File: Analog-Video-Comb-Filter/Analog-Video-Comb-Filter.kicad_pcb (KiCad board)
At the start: 2 copper layers, 51.5 x 104.1 mm, 97 parts, among them J1 12VDC(+), J2 SVHS, J3 CVBS, Q1 BC548, Q10 BC548, Q2 BC548, Q3 BC558, Q4 BC558, Q5 BC548, Q6 BC548, Q7 BC548, Q8 BC558, Q9 BC548, U1 L7805, U2 SAA4961, U3 MC44144, U4 74HC04, U5 LM1881, Y1 See table

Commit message: Replaced RCA connector footprint, added gerber files, fixed README
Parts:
- added J4: CV-IN, Custom_Footprints:Keystone_973, F.Cu at (124.2, 90.2)
- J3: value CVBS -> CV-OUT; footprint Custom_Footprints:RCA_Dual_Switch -> Custom_Footprints:Keystone_973
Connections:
- J3 pad 1: /CVBS-IN -> /CVBS-OUT
- J3 pad 3: /CVBS-OUT -> unconnected-(J3-Sw-Pad3)
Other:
- board text removed: "IN"

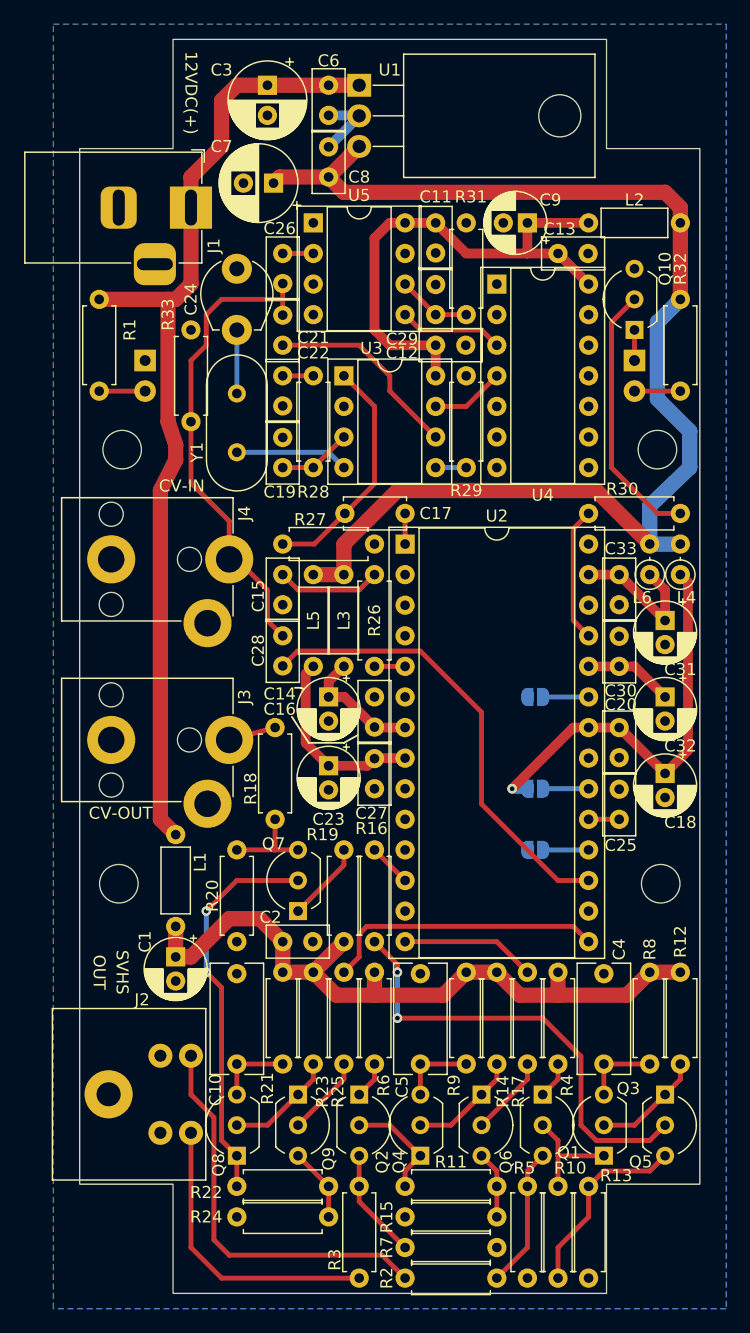
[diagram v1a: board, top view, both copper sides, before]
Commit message: Added alternative footprint for SAA4963
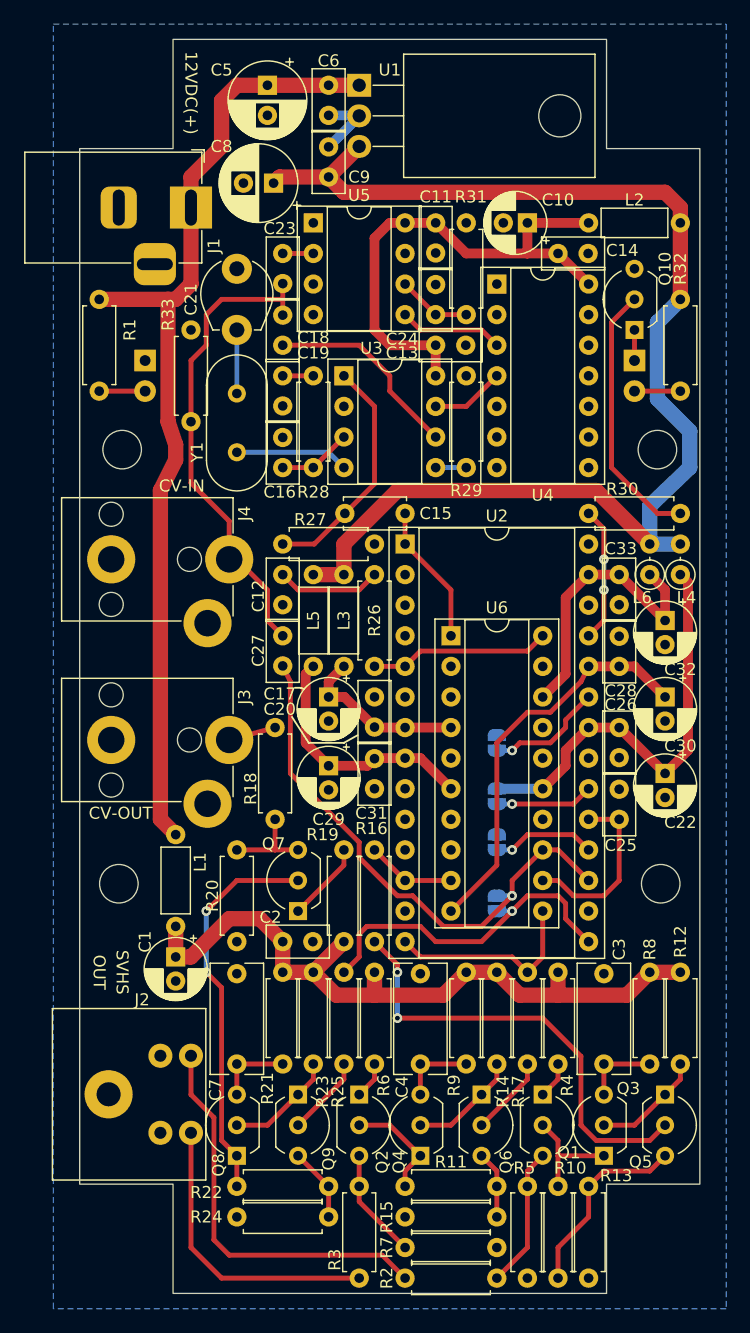
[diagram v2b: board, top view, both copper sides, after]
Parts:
- added JP4: CVBYP, Jumper:SolderJumper-2_P1.3mm_Open_RoundedPad1.0x1.5mm, B.Cu at (156.2, 118.7)
- added U6: SAA4963, Package_DIP:DIP-20_W7.62mm_Socket, F.Cu at (152.4, 96.5)
- U2: value SAA4961 -> SAA4960/61
- moved JP1 4.97 mm to (156.2, 105.4), turned to 90 degrees
- moved JP2 3.25 mm to (156.2, 109.9), turned to 90 degrees
- moved JP3 3.25 mm to (156.2, 113.7), turned to 90 degrees
- renumbered C9 to C10, C15 to C12, C12 to C13, C13 to C14, C17 to C15, C19 to C16, C14 to C17, C21 to C18, C22 to C19, C16 to C20, C24 to C21, C18 to C22, C26 to C23, C29 to C24, C20 to C26, C28 to C27, C30 to C28, C23 to C29, C4 to C3, C32 to C30, C27 to C31, C31 to C32, C5 to C4, C3 to C5, C10 to C7, C7 to C8, C8 to C9
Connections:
- net /DRV-C renamed /CO
- net /DRV-CV renamed /CVBSO
- net /DRV-Y renamed /YO
- net Net-(U2-CSY) renamed /CSY
- net Net-(U2-FSC) renamed /FSC
- net Net-(U2-REFBP) renamed /REFBP
- net Net-(U2-YEXT/CVBS) renamed /CVBS
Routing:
- net /REFDL: track 7.40 -> 33.5 mm
- net /REFBP: track 2.54 -> 15.0 mm
- net /CSY: track 2.54 -> 15.0 mm
- net +5VL: track 12.3 -> 24.0 mm
- net /FSC: track 2.54 -> 11.7 mm
- net /CVBS: track 38.3 -> 45.5 mm, vias 0 -> 1
- net Net-(JP1-A): track 3.78 -> 9.84 mm, vias 0 -> 1
- net /YO: track 11.2 -> 16.8 mm
- net /CVBSO: track 23.5 -> 28.7 mm, vias 0 -> 1
- net Net-(JP3-A): track 3.78 -> 8.68 mm, vias 0 -> 1
- net +5VP: track 15.9 -> 20.8 mm
- net +5VA: track 10.5 -> 14.9 mm
- net Net-(JP2-A): track 3.78 -> 8.15 mm, vias 0 -> 1
- net /CO: track 3.59 -> 7.40 mm
- net +5VD: track 35.2 -> 36.0 mm, vias 1 -> 0
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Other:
- board text added: "SAA4960 / SAA4961 Analog Video Comb Filter - github.com/goscickiw"
- board text removed: "SAA4960 / SAA4961 Analog Video Comb Filter github.com/goscickiw"

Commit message: Improved PCB layout, readme improvements
- Minimized (unfortunately not eliminated) ground plane interruptions under signal traces.
- Added dedicated location for SAA4963 alternative footprint REFDL filter capacitors. This way they are not far away and the trace to them is not in the way of other traces.
- Better routing of some traces around the SAA4963 alternative footprint.
- More accurate description of PLL tuning method, with pictures.
- Better quality comparison pictures.
- Various other readme fixes.
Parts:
- added C34: 100nF, Capacitor_THT:C_Disc_D5.0mm_W2.5mm_P2.50mm, F.Cu at (152.4, 118.1)
- added C35: 100uF, Capacitor_THT:CP_Radial_D5.0mm_P2.00mm, F.Cu at (157.5, 118.7)
- moved JP1 5.73 mm to (156.2, 99.7)
- moved JP4 5.12 mm to (161.3, 119.4)
- moved JP2 5.09 mm to (156.2, 104.8)
- moved U6 5.08 mm to (152.4, 91.4)
- moved R30 2.54 mm to (161.3, 86.4)
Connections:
- U6 pad 10: /REFDL -> /REFDL_63
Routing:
- net /REFDL: track 33.5 -> 7.40 mm
- net /YO: track 16.8 -> 31.8 mm
- net /CVBS: track 45.5 -> 54.7 mm
- net /REFDL_63: track 0.00 -> 9.11 mm
- net /CSY: track 15.0 -> 6.35 mm
- net Net-(U2-COMBENA): track 11.2 -> 19.7 mm, vias 2 -> 0
- net Net-(Q7-B): track 32.6 -> 40.5 mm, vias 2 -> 0
- net /REFBP: track 15.0 -> 19.4 mm
- net +5VL: track 24.0 -> 19.7 mm
- net /FSC: track 11.7 -> 7.40 mm
- net /CO: track 7.40 -> 11.0 mm
- net /CVBSO: track 28.7 -> 25.4 mm
- net +5VD: track 36.0 -> 33.1 mm, vias 0 -> 1
- net Net-(U3-XTAL): track 9.42 -> 11.7 mm, vias 0 -> 1
- net +5VA: track 14.9 -> 17.1 mm
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
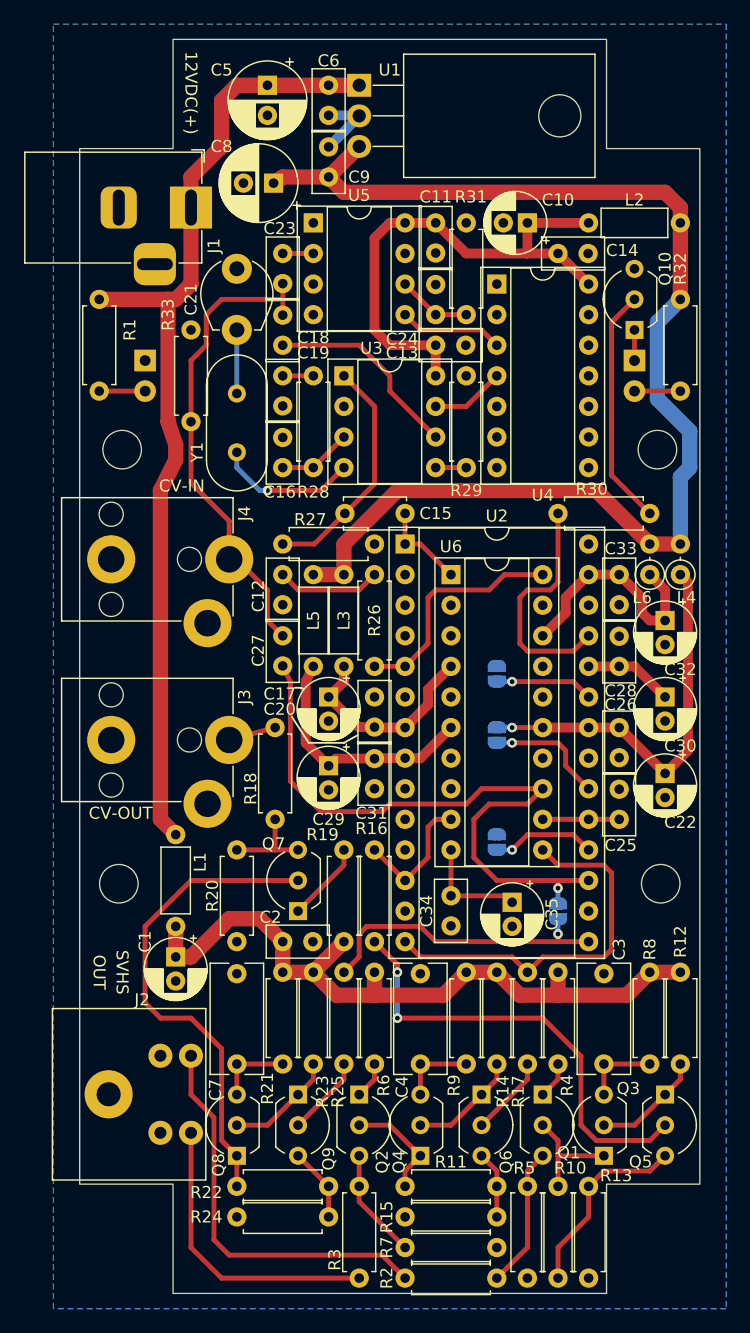
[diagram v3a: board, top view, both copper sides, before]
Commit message: New output amplifier design
The BJT amplifiers have been replaced with high bandwidth rail-to-rail operational amplifiers. This should resolve the issue of the signal becoming malformed when load is connected through a capacitor, and maybe improve the frequency response as well. The old design has been moved to "rev1-bjt-output-amplifier" branch.
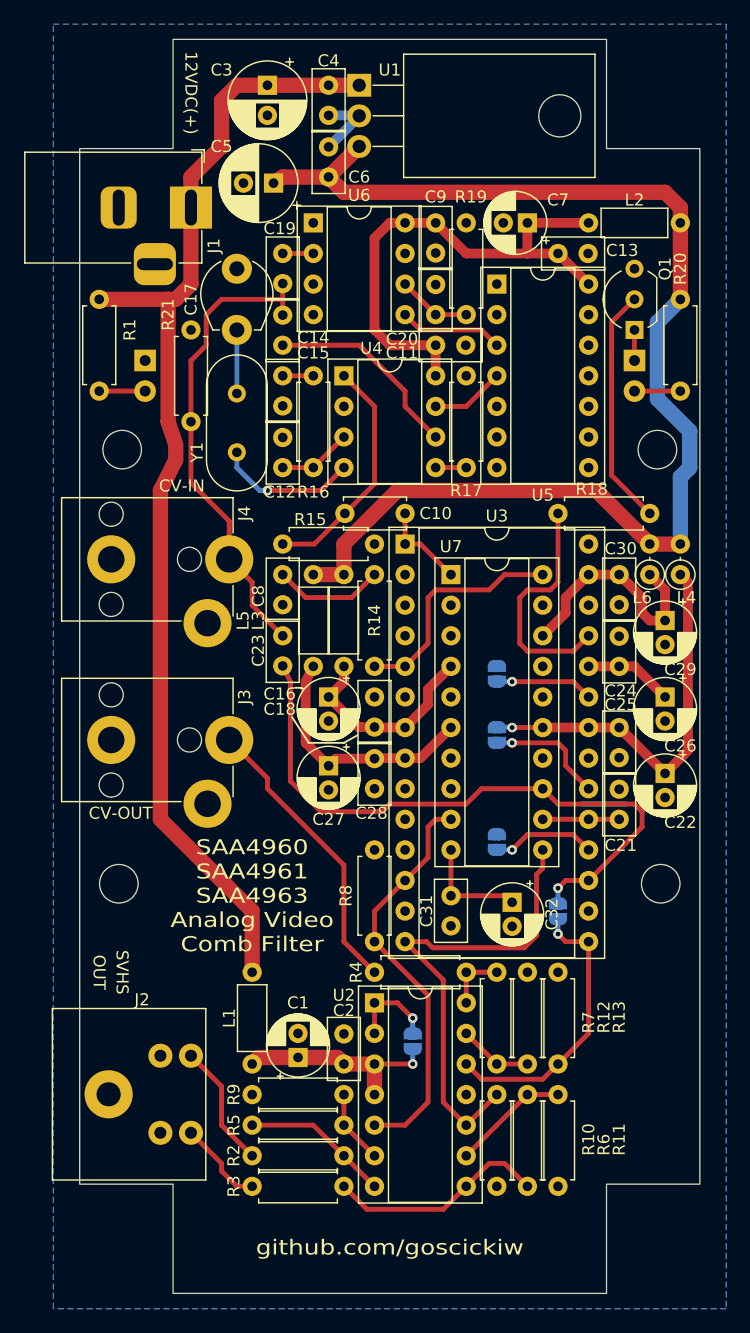
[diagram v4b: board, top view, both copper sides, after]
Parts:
- removed the C3 at (165.1, 124.6)
- removed the C4 at (149.9, 124.6)
- removed the C7 at (134.6, 124.6)
- removed the Q1 at (160.0, 134.6)
- removed Q2, Q5, Q6, Q7, Q9: BC548, Package_TO_SOT_THT:TO-92_Inline_Wide
- removed Q3, Q4, Q8: BC558, Package_TO_SOT_THT:TO-92_Inline_Wide
- removed the R14 at (156.2, 132.1)
- removed the R15 at (148.6, 144.8)
- removed the R16 at (146.1, 121.9)
- removed the R17 at (158.8, 132.1)
- removed the R18 at (137.8, 104.1)
- removed the R19 at (143.5, 114.3)
- removed the R20 at (134.6, 121.9)
- removed the R21 at (138.4, 132.1)
- removed R22, R24: 560R, Resistor_THT:R_Axial_DIN0207_L6.3mm_D2.5mm_P7.62mm_Horizontal
- removed R23: 4,7k, Resistor_THT:R_Axial_DIN0207_L6.3mm_D2.5mm_P7.62mm_Horizontal
- removed R25: 1k, Resistor_THT:R_Axial_DIN0207_L6.3mm_D2.5mm_P7.62mm_Horizontal
- added JP1: ALT, Jumper:SolderJumper-2_P1.3mm_Open_RoundedPad1.0x1.5mm, B.Cu at (149.2, 130.2)
- added U2: AD8044, Package_DIP:DIP-14_W7.62mm_Socket, F.Cu at (146.1, 127.0)
- R10: value 560R -> 10k
- R11, R13: value 560R -> 1k
- R12: value 4,7k -> 10k
- R4: value 27R -> 75R
- R6: value 27R -> 1k
- R8: value 47R -> 10k
- R9: value 47R -> 1k
- moved R5 26.2 mm to (135.9, 137.2), turned to 0 degrees
- moved R8 25.0 mm to (146.1, 121.9)
- moved R7 22.9 mm to (156.2, 124.5), turned to -90 degrees
- moved R13 18.5 mm to (158.8, 132.1)
- moved R4 17.0 mm to (146.1, 124.5), turned to 0 degrees
- moved R2 16.3 mm to (135.9, 139.7)
- moved R6 16.3 mm to (158.8, 142.2)
- moved R11 14.8 mm to (161.3, 134.6), turned to -90 degrees
- moved C1 13.2 mm to (139.7, 131.5), turned to 90 degrees
- moved L1 13.1 mm to (135.9, 124.5)
- moved R3 11.7 mm to (135.9, 142.2), turned to 0 degrees
- moved C2 11.4 mm to (143.5, 132.1), turned to 90 degrees
- moved R9 10.5 mm to (143.5, 134.6), turned to 180 degrees
- moved R12 10.2 mm to (161.3, 132.1)
- moved R10 9.16 mm to (156.2, 134.6)
- renumbered C15 to C10, C13 to C11, C16 to C12, C14 to C13, C18 to C14, C19 to C15, C17 to C16, C21 to C17, C20 to C18, C23 to C19, C24 to C20, C25 to C21, C27 to C23, C28 to C24, C26 to C25, C30 to C26, C29 to C27, C31 to C28, C32 to C29, C5 to C3, C33 to C30, C34 to C31, C35 to C32, C6 to C4, C8 to C5, C9 to C6, C10 to C7, C12 to C8, C11 to C9, JP1 to JP2, JP2 to JP3, JP3 to JP4, JP4 to JP5, Q10 to Q1, R26 to R14, R27 to R15, R28 to R16, R29 to R17, R30 to R18, R31 to R19, R32 to R20, R33 to R21, U2 to U3, U3 to U4, U4 to U5, U5 to U6, U6 to U7
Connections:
- net /C renamed /CL
- net /CVBS renamed /CV
- net /CVBS-IN renamed /CV-IN
- net /Y renamed /YL
- J3 pad 1: /CVBS-OUT -> /CVL
- JP5 pad 1: /CVBSO -> /CVO
- R10 pad 1: Net-(Q1-B) (its old number) -> /YO
- R10 pad 2: Net-(Q5-E) -> GND
- R11 pad 1: Net-(Q2-B) -> Net-(U2C--)
- R11 pad 2: Net-(Q6-E) -> GND
- R12 pad 1: Net-(Q3-B) -> /CVO
- R12 pad 2: +12VA -> GND
- R13 pad 1: GND -> Net-(U2D--)
- R13 pad 2: Net-(Q5-E) -> GND
- R2 pad 2: Net-(Q1-E) -> Net-(R2-Pad2)
- R3 pad 2: Net-(Q2-E) -> Net-(R3-Pad2)
- R4 pad 1: Net-(Q1-C) -> /CVL
- R4 pad 2: +12VA -> Net-(R4-Pad2)
- R5 pad 1: GND -> Net-(R2-Pad2)
- R5 pad 2: Net-(Q1-E) -> Net-(U2B--)
- R6 pad 1: Net-(Q2-C) -> Net-(R3-Pad2)
- R6 pad 2: +12VA -> Net-(U2C--)
- R7 pad 1: GND -> Net-(R4-Pad2)
- R7 pad 2: Net-(Q2-E) -> Net-(U2D--)
- R8 pad 1: Net-(Q3-E) -> /CO
- R8 pad 2: +12VA -> GND
- R9 pad 1: Net-(Q4-E) -> Net-(U2B--)
- R9 pad 2: +12VA -> GND
- U3 pad 15: /CVBSO -> /CVO
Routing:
- net +12VA: track 59.7 -> 17.6 mm, vias 0 -> 1
- net Net-(Q7-B): track 40.5 -> 0.00 mm
- net Net-(Q5-B): track 37.4 -> 0.00 mm, vias 2 -> 0
- net /CVBSO: track 25.4 -> 0.00 mm, vias 1 -> 0
- net /CVL: track 0.00 -> 24.3 mm
- net /CVO: track 0.00 -> 23.9 mm, vias 0 -> 1
- net /CO: track 11.0 -> 33.9 mm
- net /CL: track 33.3 -> 10.4 mm
- net Net-(R3-Pad2): track 0.00 -> 18.4 mm
- net /YL: track 24.5 -> 7.29 mm
- net Net-(Q5-E): track 16.1 -> 0.00 mm
- net +12V: track 81.8 -> 95.8 mm
- net Net-(R2-Pad2): track 0.00 -> 12.3 mm
- net Net-(Q1-E): track 11.7 -> 0.00 mm
- net Net-(U2C--): track 0.00 -> 9.72 mm
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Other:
- board text added: "SAA4960 SAA4961 SAA4963 Analog Video Comb Filter"
- board text added: "github.com/goscickiw"
- board text removed: "SAA4960 / SAA4961 Analog Video Comb Filter - github.com/goscickiw"
